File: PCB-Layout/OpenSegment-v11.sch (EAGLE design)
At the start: 46 parts, among them Q1 PNP, Q10 MMBT2222, Q11 MMBT2222, Q12 MMBT2222, Q2 PNP, Q3 PNP, Q4 PNP, Q5 PNP, Q6 PNP, Q7 PNP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

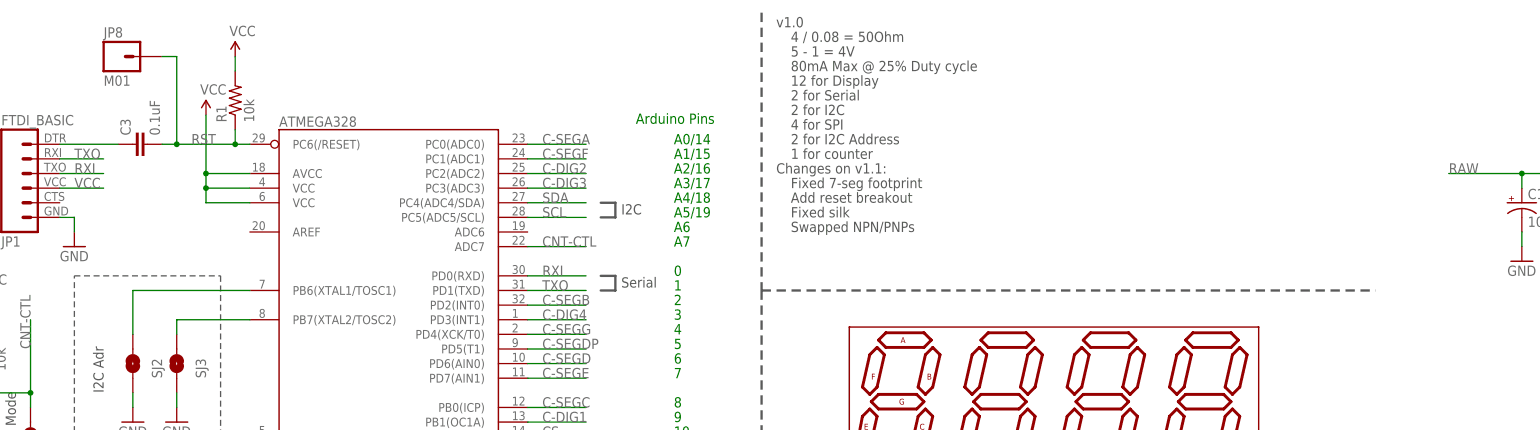
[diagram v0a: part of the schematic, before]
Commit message: Changing v1.2 of the PCB.
Dropped I2C jumpers. Added analog pins. Thinking about added mode select
jumpers.
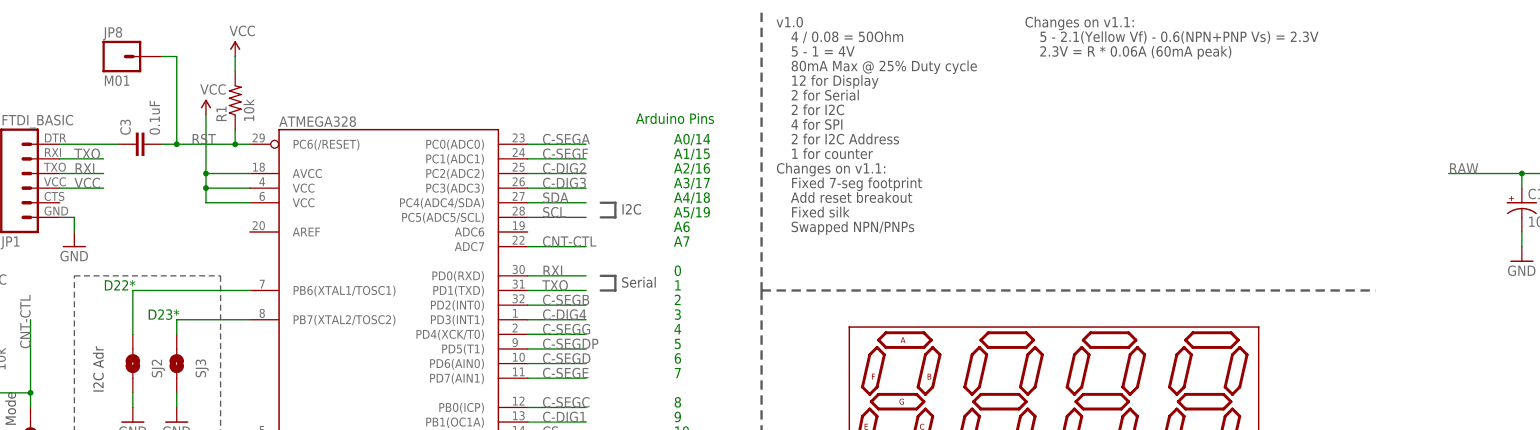
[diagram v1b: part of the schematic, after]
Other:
- note added: "2.3V = R * 0.06A (60mA peak)"
- note added: "5 - 2.1(Yellow Vf) - 0.6(NPN+PNP Vs) = 2.3V"
- note added: "D22*"
- note added: "D23*"
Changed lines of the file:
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@@
 <?xml version="1.0" encoding="utf-8"?>
 <!DOCTYPE eagle SYSTEM "eagle.dtd">
-<eagle version="6.2">
+<eagle version="6.3">
 <drawing>
 <settings>
@@
 <text x="147.32" y="149.86" size="1.778" layer="97">Fixed silk</text>
 <text x="147.32" y="147.32" size="1.778" layer="97">Swapped NPN/PNPs</text>
+<text x="27.94" y="137.16" size="1.778" layer="91">D22*</text>
+<text x="35.56" y="132.08" size="1.778" layer="91">D23*</text>
+<text x="190.5" y="180.34" size="1.778" layer="97">5 - 2.1(Yellow Vf) - 0.6(NPN+PNP Vs) = 2.3V</text>
+<text x="190.5" y="177.8" size="1.778" layer="97">2.3V = R * 0.06A (60mA peak)</text>
+<text x="187.96" y="182.88" size="1.778" layer="97">Changes on v1.1:</text>
 </plain>
 <instances>
